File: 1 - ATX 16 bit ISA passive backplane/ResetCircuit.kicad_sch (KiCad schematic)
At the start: 32 parts, among them U1 74HCT14, U3 74HCT74

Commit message: Finally finalized the backplane to my liking.
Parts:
- removed D?: POWER, LED_THT:LED_D3.0mm, symbol Device:LED
- removed D?: RESET, LED_THT:LED_D3.0mm, symbol Device:LED
- removed J?: PWR LED, 0_Library:PinHeader_1x2_Vertical (Modified), symbol Connector_Generic:Conn_01x02
- removed J?: RST LED, 0_Library:PinHeader_1x2_Vertical (Modified), symbol Connector_Generic:Conn_01x02
- removed J?: RST SW, 0_Library:PinHeader_1x2_Vertical (Modified), symbol Connector_Generic:Conn_01x02
- removed R? (x3): 220, Resistor_THT:R_Axial_DIN0207_L6.3mm_D2.5mm_P10.16mm_Horizontal, symbol Device:R_US
- removed R?: 330, Resistor_THT:R_Axial_DIN0207_L6.3mm_D2.5mm_P10.16mm_Horizontal, symbol Device:R_US
- removed SW?: RESET, Button_Switch_THT:SW_PUSH-12mm, symbol Switch:SW_Push
- added C? (x2): 1µF, Capacitor_THT:C_Disc_D3.0mm_W1.6mm_P2.50mm, symbol Device:C
- added J?: RST_SW, 0_Library:PinHeader_1x2_Vertical (Modified), symbol Connector_Generic:Conn_01x02
- added J?: ACTIVITY ADDR, Connector_PinHeader_2.54mm:PinHeader_1x03_P2.54mm_Vertical, symbol Connector_Generic:Conn_01x03
- added J?: RST_LED, 0_Library:PinHeader_1x2_Vertical (Modified), symbol Connector_Generic:Conn_01x02
- added R?: 220, Resistor_THT:R_Axial_DIN0207_L6.3mm_D2.5mm_P10.16mm_Horizontal, symbol Device:R_US
- added R?: 330, Resistor_THT:R_Axial_DIN0207_L6.3mm_D2.5mm_P10.16mm_Horizontal, symbol Device:R_US
- added SW?: RESET, 0_Library:Pushbutton_12mm_LED, symbol Switch:SW_Push_LED
- added U?: 74HCT14, Package_DIP:DIP-14_W7.62mm, symbol 74xx:74HC14
- added U?: 74HCT74, Package_DIP:DIP-14_W7.62mm, symbol 74xx:74HC74
- C?: value 0.1µF -> 1µF
- J?: value RST POL -> RST POLARITY
- R?: value 330 -> 2K2
- renumbered D4 to D2, U3 to U?, U1 to U?
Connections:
- net -RST: now also J?.2 (Pin_2), SW?.2
- net A8: now also J?.3 (Pin_3); no longer U?.3 (C)
- net GND: now also C?.2, C?.2, J?.1 (Pin_1), J?.2 (Pin_2), SW?.1, SW?.3 (K), U?.7 (GND), U?.7 (GND)
- net at U?.8: now also R?.2, R?.2
- new net: J?.2 (Pin_2), U?.3 (C)
- new net: J?.1 (Pin_1), R?.1
- new net: R?.1, SW?.4 (A)
- new net A7: J?.1 (Pin_1)
- new net VCC: C?.1, C?.1, U?.14 (VCC), U?.14 (VCC)
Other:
- note added: "Bypass Capacitors"
- note removed: "Green"
- note removed: "POWER LED"
- note removed: "Red"
- moved on the sheet: C?, D2, D?, J?, R?, RS?, U?A, U?D, U?E

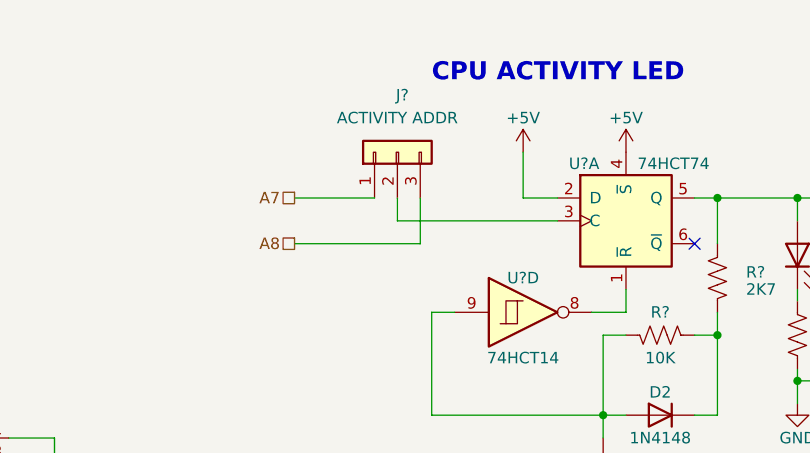
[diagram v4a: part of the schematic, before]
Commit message: Removed the alternate power input.
The soft power on circuit was flaky upon testing.
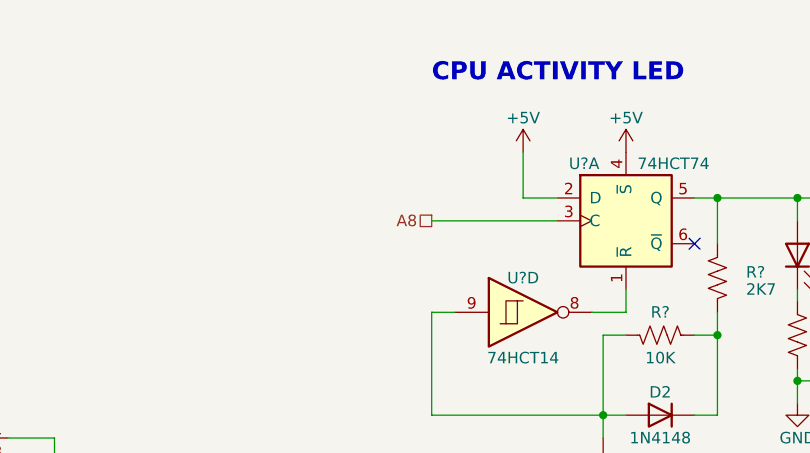
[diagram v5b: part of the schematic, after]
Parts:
- removed J?: ACTIVITY ADDR, Connector_PinHeader_2.54mm:PinHeader_1x03_P2.54mm_Vertical, symbol Connector_Generic:Conn_01x03
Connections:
- net A8: now also U?.3 (C)
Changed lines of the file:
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@@
   (title_block
     (title "Reset and CPU activity circuits")
-    (date "2023-08-21")
+    (date "2023-09-02")
     (rev "2.1")
     (company "Frederic Segard  (@microhobbyist)")
@@
     (stroke (width 0) (type default))
   )
-  (wire (pts (xy 163.83 46.99) (xy 163.83 49.53))
-    (stroke (width 0) (type default))
-  )
   (wire (pts (xy 107.95 69.85) (xy 60.96 69.85))
     (stroke (width 0) (type default))
@@
     (stroke (width 0) (type default))
   )
-  (wire (pts (xy 152.4 52.07) (xy 166.37 52.07))
+  (wire (pts (xy 167.64 49.53) (xy 181.61 49.53))
     (stroke (width 0) (type default))
   )
@@
     (stroke (width 0) (type default))
   )
-  (wire (pts (xy 152.4 46.99) (xy 161.29 46.99))
-    (stroke (width 0) (type default))
-  )
   (wire (pts (xy 107.95 73.66) (xy 107.95 69.85))
     (stroke (width 0) (type default))
   )
   (wire (pts (xy 189.23 62.23) (xy 186.69 62.23))
-    (stroke (width 0) (type default))
-  )
-  (wire (pts (xy 163.83 49.53) (xy 181.61 49.53))
-    (stroke (width 0) (type default))
-  )
-  (wire (pts (xy 166.37 52.07) (xy 166.37 46.99))
     (stroke (width 0) (type default))
   )
@@
     (effects (font (size 1.27 1.27)) (justify left bottom))
   )
-  (hierarchical_label "A8" (shape passive) (at 152.4 52.07 180) (fields_autoplaced)
-    (effects (font (size 1.27 1.27)) (justify right))
-  )
-  (hierarchical_label "A7" (shape passive) (at 152.4 46.99 180) (fields_autoplaced)
+  (hierarchical_label "A8" (shape passive) (at 167.64 49.53 180) (fields_autoplaced)
     (effects (font (size 1.27 1.27)) (justify right))
   )
@@
         )
       )
-    )
-  )
-  (symbol (lib_id "Connector_Generic:Conn_01x03") (at 163.83 41.91 90) (unit 1)
-    (in_bom yes) (on_board yes) (dnp no)
-    (property "Reference" "J?" (at 165.1 35.56 90)
-      (effects (font (size 1.27 1.27)) (justify left))
-    )
-    (property "Value" "ACTIVITY ADDR" (at 163.83 38.1 90)
-      (effects (font (size 1.27 1.27)))
-    )
-    (property "Footprint" "Connector_PinHeader_2.54mm:PinHeader_1x03_P2.54mm_Vertical" (at 163.83 41.91 0)
-      (effects (font (size 1.27 1.27)) hide)
-    )
-    (property "Datasheet" "~" (at 163.83 41.91 0)
-      (effects (font (size 1.27 1.27)) hide)
-    )
-    (pin "1")
-    (pin "2")
-    (pin "3")
-    (instances
-      (project "1 - ATX 16 bit ISA passive backplane"
-        (path "/8a50abe0-5000-47f3-b1a5-f37ea7324f50/184965a6-7940-44d4-8637-f93e65786f3f"
-          (reference "J?") (unit 1)
-        )
-        (path "/8a50abe0-5000-47f3-b1a5-f37ea7324f50/7fc482b2-248e-46ca-8eac-60e4e514a973"
-          (reference "J21") (unit 1)
-        )
-      )
